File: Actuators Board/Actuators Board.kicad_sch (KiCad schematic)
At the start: 83 parts, among them IC1 BD62120AEFJ-E2, J1 Conn_01x05_Male, J10 Conn_01x02_Male, J2 Solenoid(Sol), J4 Conn_01x03_Male, J5 Conn_01x06_Male, J9 Conn_01x02_Male, Q1 MMDT2222A, Q2 SI2366DS, U1 ESP32-PICO-D4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

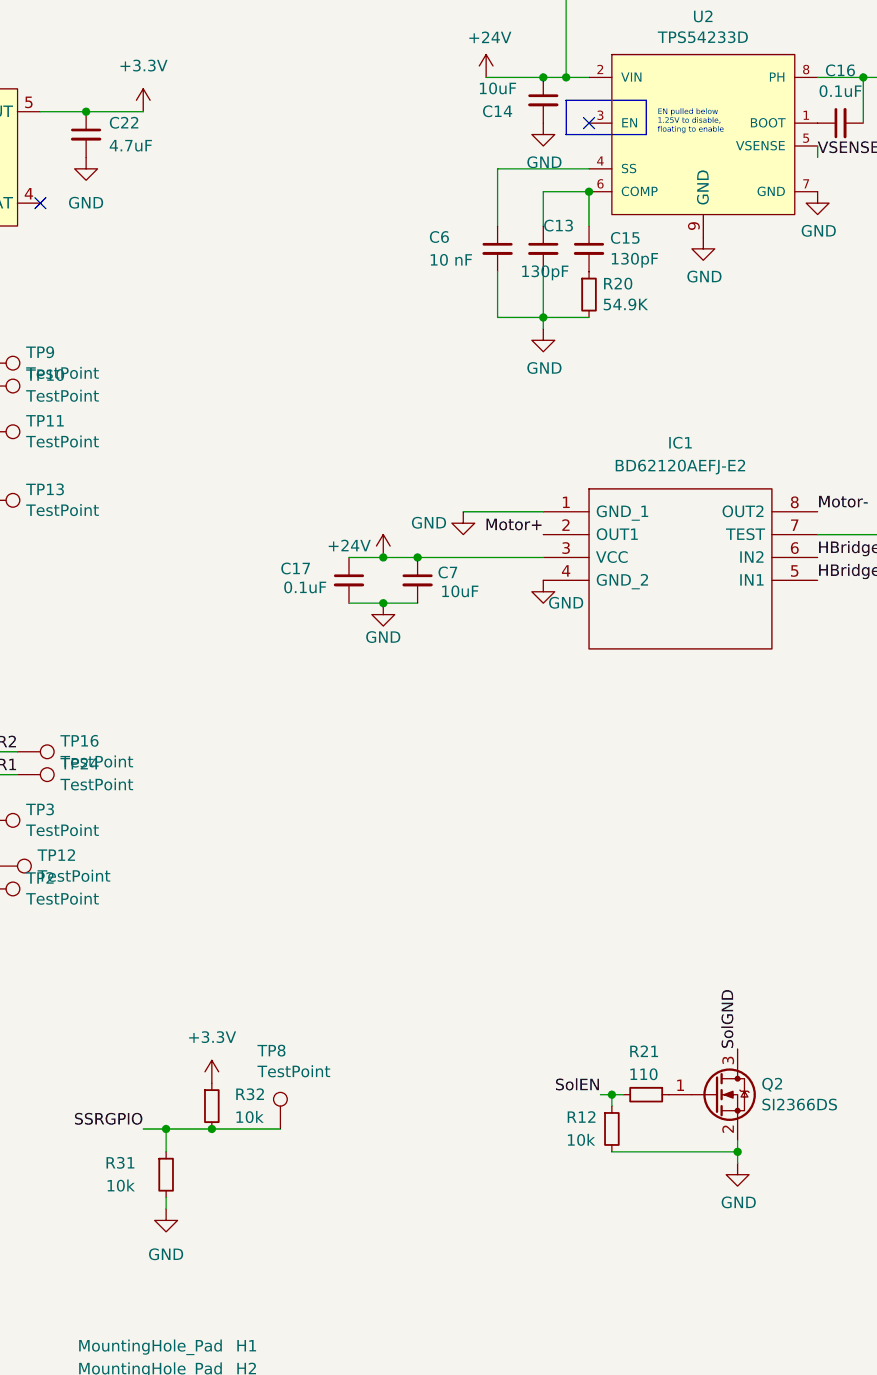
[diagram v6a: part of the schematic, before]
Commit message: Swapped SSR pad for connector
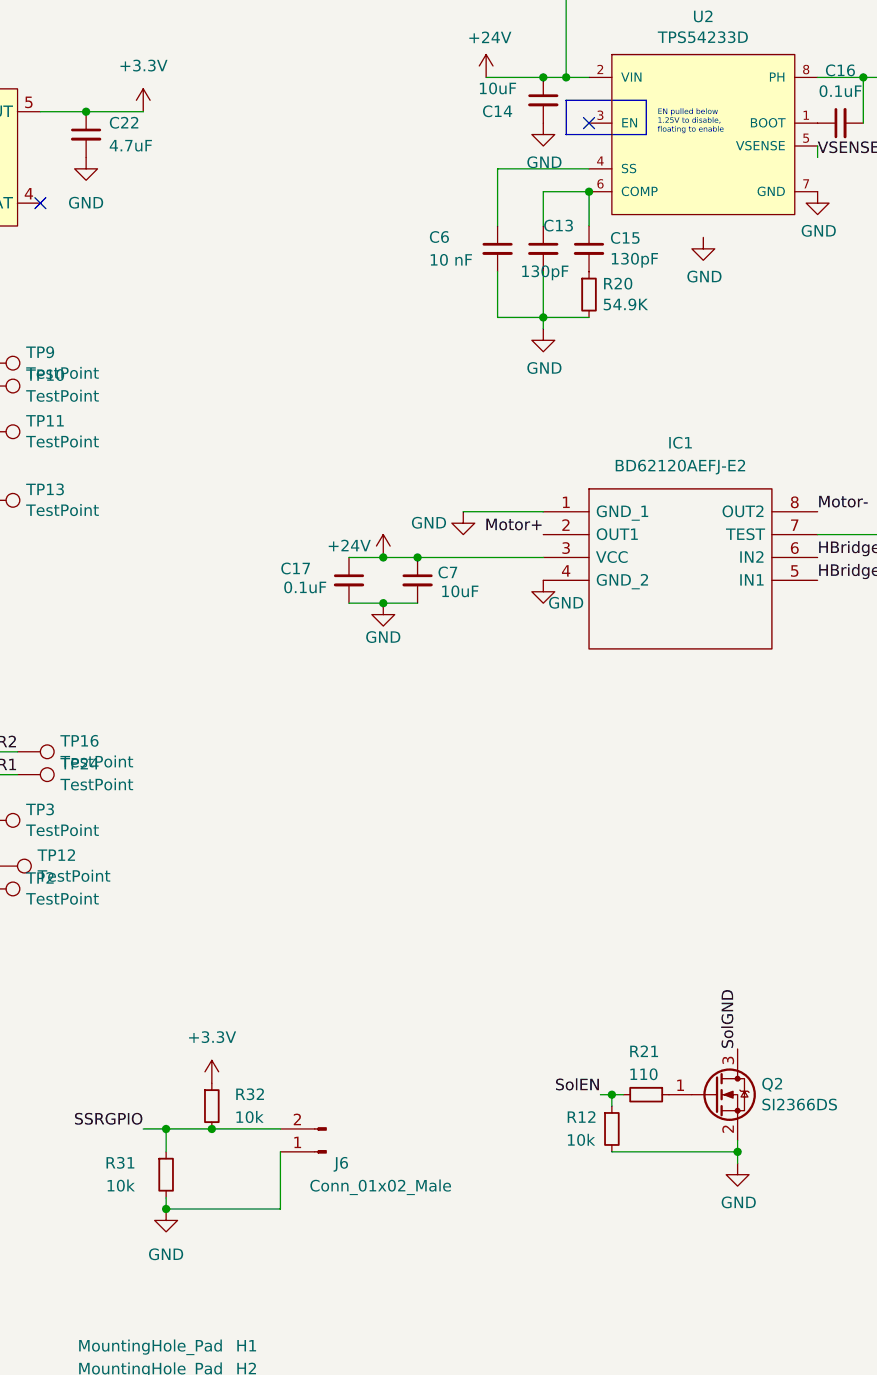
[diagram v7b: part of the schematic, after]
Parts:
- removed TP8: TestPoint, TestPoint:TestPoint_Pad_D1.5mm, symbol Connector:TestPoint
- added J6: Conn_01x02_Male, Connector_PinHeader_2.54mm:PinHeader_1x02_P2.54mm_Vertical, symbol Connector:Conn_01x02_Male
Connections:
- net GND: now also J6.1 (Pin_1); no longer U2.9 (GND)
- net SSRGPIO: now also J6.2 (Pin_2)
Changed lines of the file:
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@@
   (junction (at 187.96 92.71) (diameter 0) (color 0 0 0 0)
   )
+  (junction (at 163.83 160.02) (diameter 0) (color 0 0 0 0)
+  )
   (junction (at 99.06 45.72) (diameter 0) (color 0 0 0 0)
   )
@@
     (stroke (width 0) (type default) (color 0 0 0 0))
   )
+  (wire (pts (xy 163.83 160.02) (xy 176.53 160.02))
+    (stroke (width 0) (type default) (color 0 0 0 0))
+  )
   (wire (pts (xy 91.44 45.72) (xy 91.44 46.99))
     (stroke (width 0) (type default) (color 0 0 0 0))
@@
     (stroke (width 0) (type default) (color 0 0 0 0))
   )
+  (wire (pts (xy 176.53 160.02) (xy 176.53 153.67))
+    (stroke (width 0) (type default) (color 0 0 0 0))
+  )
   (wire (pts (xy 236.22 85.09) (xy 250.19 85.09))
     (stroke (width 0) (type default) (color 0 0 0 0))
@@
     (pin "7")
     (pin "8")
-    (pin "9")
   )
   (symbol (lib_id "power:GND") (at 236.22 46.99 0) (unit 1)
@@
     (pin "2")
   )
+  (symbol (lib_id "Connector:Conn_01x02_Male") (at 181.61 153.67 180) (unit 1)
+    (in_bom yes) (on_board yes)
+    (property "Reference" "J6" (id 0) (at 184.15 154.94 0)
+      (effects (font (size 1.27 1.27)) (justify left))
+    )
+    (property "Value" "Conn_01x02_Male" (id 1) (at 195.58 157.48 0)
+      (effects (font (size 1.27 1.27)) (justify left))
+    )
+    (property "Footprint" "Connector_PinHeader_2.54mm:PinHeader_1x02_P2.54mm_Vertical" (id 2) (at 181.61 153.67 0)
+      (effects (font (size 1.27 1.27)) hide)
+    )
+    (property "Datasheet" "~" (id 3) (at 181.61 153.67 0)
+      (effects (font (size 1.27 1.27)) hide)
+    )
+    (pin "1")
+    (pin "2")
+  )
   (symbol (lib_id "Device:R_Small") (at 213.36 151.13 0) (unit 1)
     (in_bom yes) (on_board yes)
@@
     (pin "2")
   )
-  (symbol (lib_id "Connector:TestPoint") (at 176.53 151.13 0) (unit 1)
-    (in_bom yes) (on_board yes)
-    (property "Reference" "TP8" (id 0) (at 173.99 142.4686 0)
-      (effects (font (size 1.27 1.27)) (justify left))
-    )
-    (property "Value" "TestPoint" (id 1) (at 173.99 144.78 0)
-      (effects (font (size 1.27 1.27)) (justify left))
-    )
-    (property "Footprint" "TestPoint:TestPoint_Pad_D1.5mm" (id 2) (at 181.61 151.13 0)
-      (effects (font (size 1.27 1.27)) hide)
-    )
-    (property "Datasheet" "~" (id 3) (at 181.61 151.13 0)
-      (effects (font (size 1.27 1.27)) hide)
-    )
-    (pin "1")
-  )
   (symbol (lib_id "power:GND") (at 205.74 90.17 0) (unit 1)
     (in_bom yes) (on_board yes)
@@
       (reference "J5") (unit 1) (value "Conn_01x06_Male") (footprint "Connector_Molex:Molex_Nano-Fit_105309-xx06_1x06_P2.50mm_Vertical")
     )
+    (path "/11cdec55-435f-4b7f-805a-bee9ab2b00ee"
+      (reference "J6") (unit 1) (value "Conn_01x02_Male") (footprint "Connector_PinHeader_2.54mm:PinHeader_1x02_P2.54mm_Vertical")
+    )
     (path "/00000000-0000-0000-0000-00005dff606f"
       (reference "J9") (unit 1) (value "Conn_01x02_Male") (footprint "Connector_PinHeader_2.54mm:PinHeader_1x02_P2.54mm_Vertical")
@@
       (reference "TP5") (unit 1) (value "TestPoint") (footprint "TestPoint:TestPoint_Pad_D1.0mm")
     )
-    (path "/7b493daa-00cc-424e-8a6c-f99c2e08ae97"
-      (reference "TP8") (unit 1) (value "TestPoint") (footprint "TestPoint:TestPoint_Pad_D1.5mm")
-    )
     (path "/00000000-0000-0000-0000-000061b1d3c4"

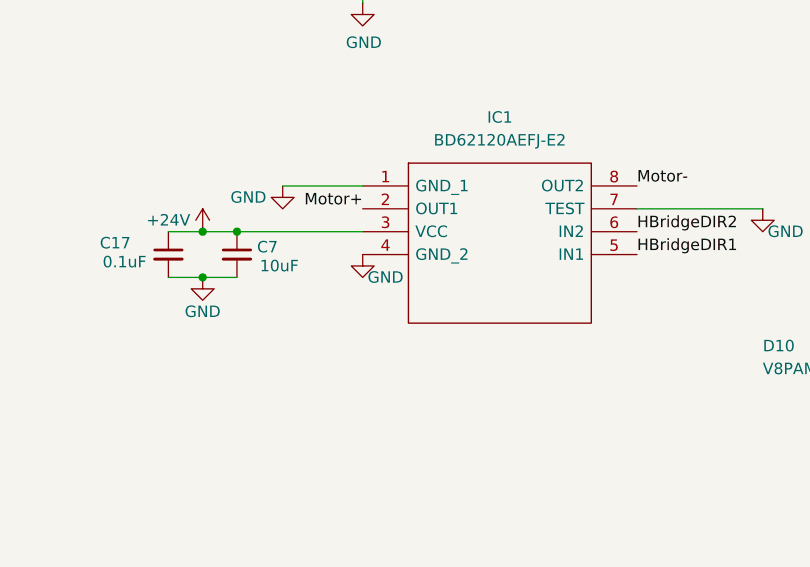
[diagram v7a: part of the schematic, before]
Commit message: Fixed front silkscreen (references) and added ICLR logo + designer names
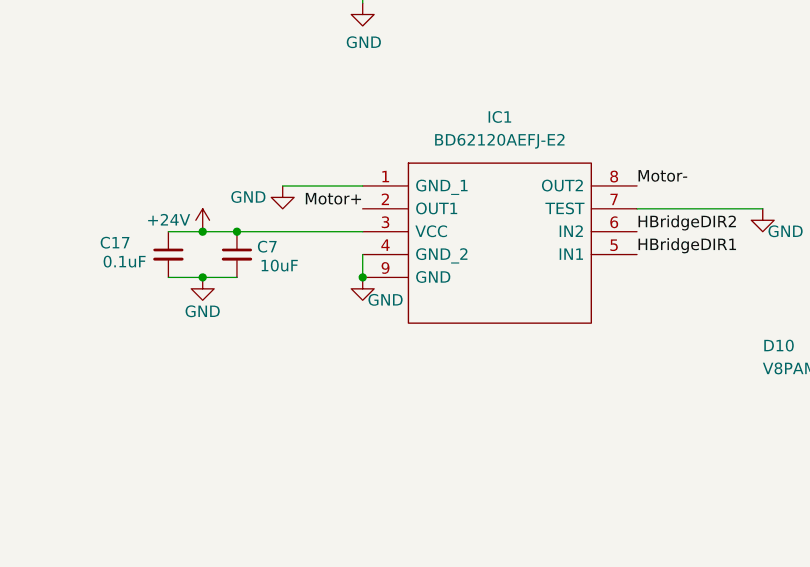
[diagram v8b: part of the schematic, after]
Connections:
- net GND: now also IC1.9 (GND)
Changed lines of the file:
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@@
   (junction (at 99.06 45.72) (diameter 0) (color 0 0 0 0)
+  )
+  (junction (at 205.74 92.71) (diameter 0) (color 0 0 0 0)
   )
   (junction (at 205.74 34.29) (diameter 0) (color 0 0 0 0)
@@
   )
   (wire (pts (xy 114.3 137.16) (xy 114.3 142.24))
+    (stroke (width 0) (type default) (color 0 0 0 0))
+  )
+  (wire (pts (xy 205.74 92.71) (xy 205.74 90.17))
     (stroke (width 0) (type default) (color 0 0 0 0))
   )
@@
     (pin "2")
   )
-  (symbol (lib_id "power:GND") (at 205.74 90.17 0) (unit 1)
-    (in_bom yes) (on_board yes)
-    (property "Reference" "#PWR0134" (id 0) (at 205.74 96.52 0)
-      (effects (font (size 1.27 1.27)) hide)
-    )
-    (property "Value" "GND" (id 1) (at 208.28 92.71 0))
-    (property "Footprint" "" (id 2) (at 205.74 90.17 0)
-      (effects (font (size 1.27 1.27)) hide)
-    )
-    (property "Datasheet" "" (id 3) (at 205.74 90.17 0)
+  (symbol (lib_id "power:GND") (at 205.74 92.71 0) (unit 1)
+    (in_bom yes) (on_board yes)
+    (property "Reference" "#PWR0134" (id 0) (at 205.74 99.06 0)
+      (effects (font (size 1.27 1.27)) hide)
+    )
+    (property "Value" "GND" (id 1) (at 208.28 95.25 0))
+    (property "Footprint" "" (id 2) (at 205.74 92.71 0)
+      (effects (font (size 1.27 1.27)) hide)
+    )
+    (property "Datasheet" "" (id 3) (at 205.74 92.71 0)
       (effects (font (size 1.27 1.27)) hide)
     )
@@
     (pin "3")
     (pin "4")
+    (pin "9")
     (pin "5")
     (pin "6")
